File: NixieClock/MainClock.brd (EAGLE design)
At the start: 160 x 50 mm, 87 parts, among them IC1 MEGA8-P, IC2 74141N, IC3 NE555, Q1 MPSA 42, Q10 IRF740, Q11 BC547, Q12 MPSA 92, Q13 MPSA 42, Q14 MPSA 42, Q15 MPSA55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

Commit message: Placed all Parts
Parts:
- moved R15 191.4 mm to (86.0, 26.0)
- moved R37 172.6 mm to (70.0, 26.0), turned to 270 degrees
- moved NEON 167.2 mm to (76.0, 30.0), turned to 270 degrees
- moved C1 166.6 mm to (68.2, 13.9)
- moved R19 163.8 mm to (84.0, 46.0), turned to 90 degrees
- moved R36 158.5 mm to (72.0, 36.0), turned to 180 degrees
- moved D1 147.7 mm to (86.0, 34.0)
- moved R29 146.7 mm to (36.0, 14.0), turned to 180 degrees
- moved R30 145.7 mm to (14.0, 4.00), turned to 180 degrees
- moved Q15 139.0 mm to (100.0, 4.00), turned to 180 degrees
- moved Q11 136.0 mm to (91.9, 45.1), turned to 90 degrees
- moved R23 134.2 mm to (14.0, 16.0)
- moved R18 132.4 mm to (78.0, 43.5), turned to 90 degrees
- moved R17 129.5 mm to (86.0, 40.0), turned to 180 degrees
- moved R13 124.5 mm to (36.0, 22.0), turned to 180 degrees
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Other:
- board size 160 x 50 mm -> 172 x 52 mm

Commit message: Began Routing
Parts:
- moved +180V(TEST) 12.0 mm to (4.00, 4.00)
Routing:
- net N$34: track 0.00 -> 155.7 mm
- net N$16: track 0.00 -> 17.7 mm
- net N$11: track 0.00 -> 13.7 mm
- net N$15: track 0.00 -> 13.3 mm
- net N$55: track 0.00 -> 12.7 mm
- net N$33: track 0.00 -> 12.7 mm
- net N$32: track 0.00 -> 12.7 mm
- net N$31: track 0.00 -> 12.7 mm
- net N$30: track 0.00 -> 12.7 mm
- net N$29: track 0.00 -> 12.7 mm
- net N$12: track 0.00 -> 9.29 mm
- net N$14: track 0.00 -> 7.01 mm
- net N$40: track 0.00 -> 6.41 mm
- net N$39: track 0.00 -> 6.41 mm
- net N$38: track 0.00 -> 6.41 mm
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- added copper zone on layer 16, net VCC

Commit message: Routed the rest w the help of autorouter
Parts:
- moved R15 3.61 mm to (88.0, 29.0)
- moved D2 2.83 mm to (100.0, 8.00)
- moved CATHODE 1.50 mm to (76.0, 15.5)
- moved IC2 1.50 mm to (86.0, 13.5)
- moved NEON 1.00 mm to (76.0, 31.0)
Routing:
- net 9V: track 0.00 -> 185.0 mm
- net DIGITAL_PIN_13: track 0.00 -> 92.0 mm, vias 0 -> 2
- net DIGITAL_PIN_8: track 0.00 -> 91.6 mm, vias 0 -> 1
- net ANALOG_0: track 0.00 -> 89.7 mm
- net DIGITAL_PIN_10: track 0.00 -> 87.1 mm, vias 0 -> 2
- net DIGITAL_PIN_12: track 0.00 -> 85.8 mm, vias 0 -> 3
- net N$34: track 155.7 -> 237.0 mm
- net DIGITAL_PIN_11: track 0.00 -> 80.3 mm, vias 0 -> 1
- net DIGITAL_PIN_9: track 0.00 -> 76.8 mm, vias 0 -> 1
- net DIGITAL_PIN_5: track 0.00 -> 67.2 mm, vias 0 -> 3
- net N$7: track 0.00 -> 66.1 mm
- net DIGITAL_PIN_4: track 0.00 -> 62.2 mm, vias 0 -> 2
- net ANALOG_1: track 0.00 -> 56.4 mm, vias 0 -> 1
- net N$62: track 0.00 -> 55.9 mm
- net DIGITAL_PIN_2: track 0.00 -> 50.2 mm
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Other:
- board size 172 x 52 mm -> 172 x 54 mm

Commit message: Added Holes
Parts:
- moved GND 48.4 mm to (56.0, 50.0)
- moved +180V(TEST) 8.25 mm to (6.00, 12.0)
- moved 9V/12-35V-DC-IN 2.83 mm to (155.7, 8.31)
- moved 12-35V/9V 2.83 mm to (168.0, 30.0)
- moved ANODE 2.83 mm to (6.00, 28.0)
- moved BUZZER 2.83 mm to (158.0, 44.0)
- moved C1 2.83 mm to (70.2, 15.9)
- moved C10 2.83 mm to (148.0, 22.0)
- moved C2 2.83 mm to (114.0, 32.0)
- moved C3 2.83 mm to (106.0, 44.0)
- moved C4 2.83 mm to (82.0, 32.0)
- moved C5 2.83 mm to (136.0, 28.0)
- moved C6 2.83 mm to (142.0, 28.0)
- moved C7 2.83 mm to (148.0, 30.0)
- moved C8 2.83 mm to (138.0, 20.0)
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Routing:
- net N$49: track 36.7 -> 39.9 mm
- net DIGITAL_PIN_12: track 85.8 -> 87.5 mm
- net N$34: track 237.0 -> 237.9 mm
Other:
- board size 172 x 54 mm -> 174 x 56 mm

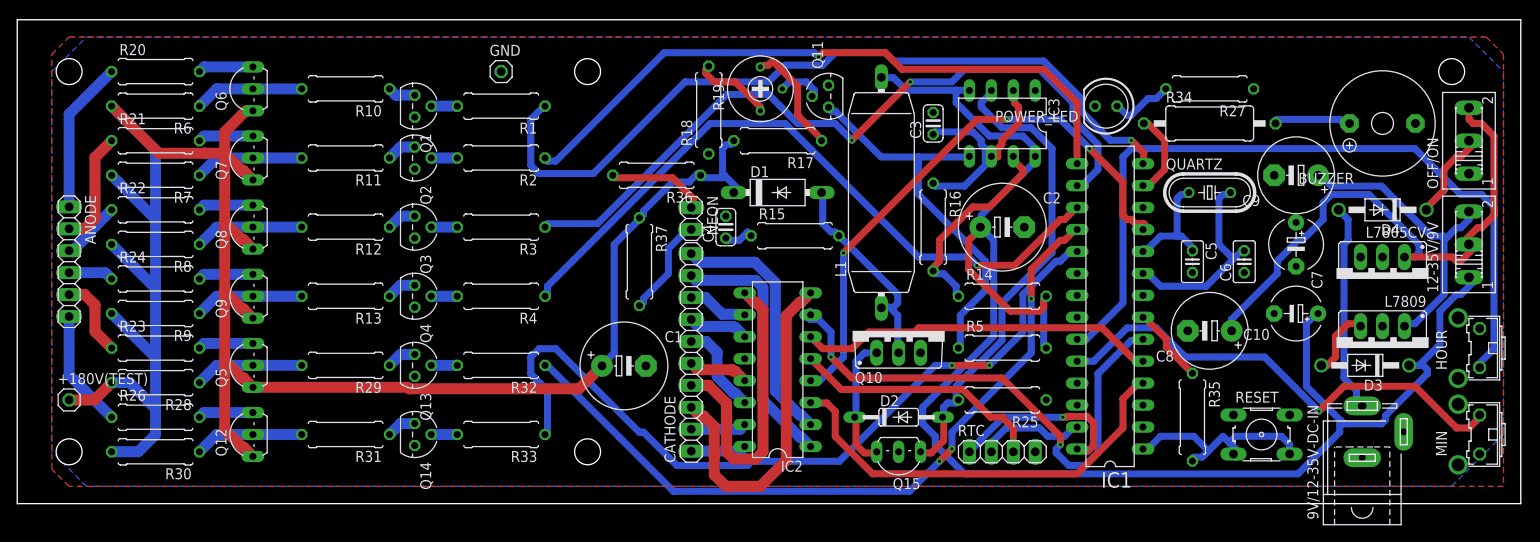
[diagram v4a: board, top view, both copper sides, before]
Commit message: Moved Names and Values so that they are easily readable
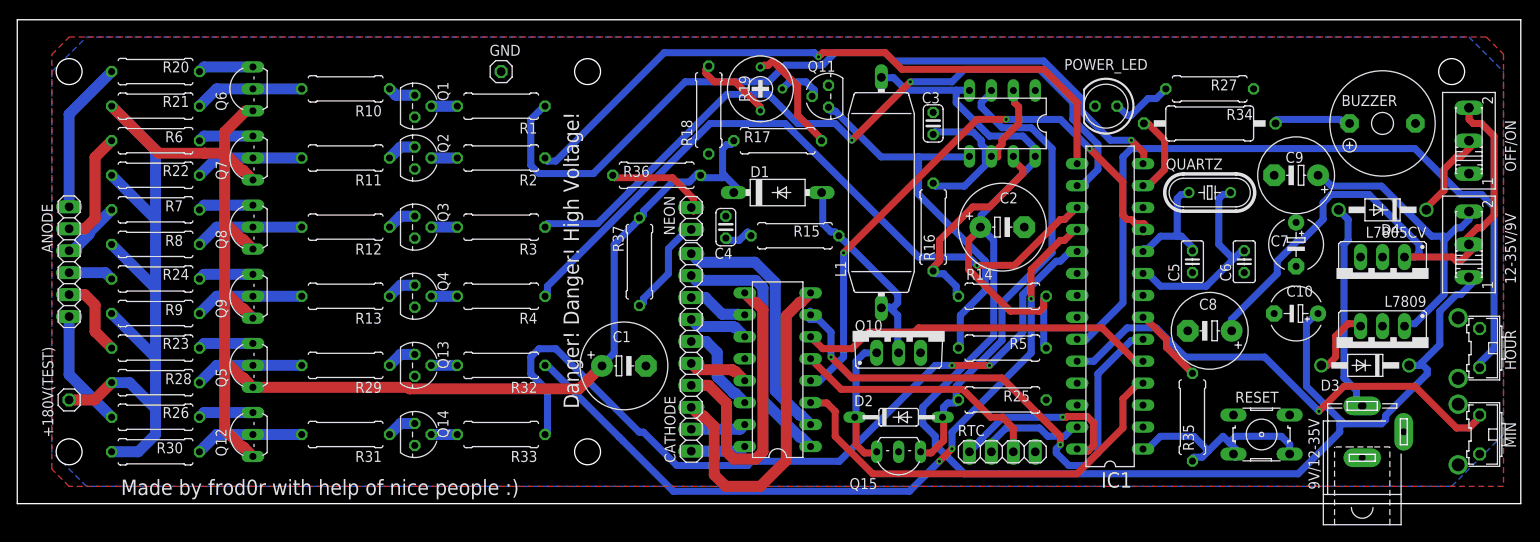
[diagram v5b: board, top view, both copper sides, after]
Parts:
- renumbered 9V/12-35V-DC-IN to 9V/12-35V
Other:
- board text added: "Danger! Danger! High Voltage!"
- board text added: "Made by frod0r with help of nice people :)"

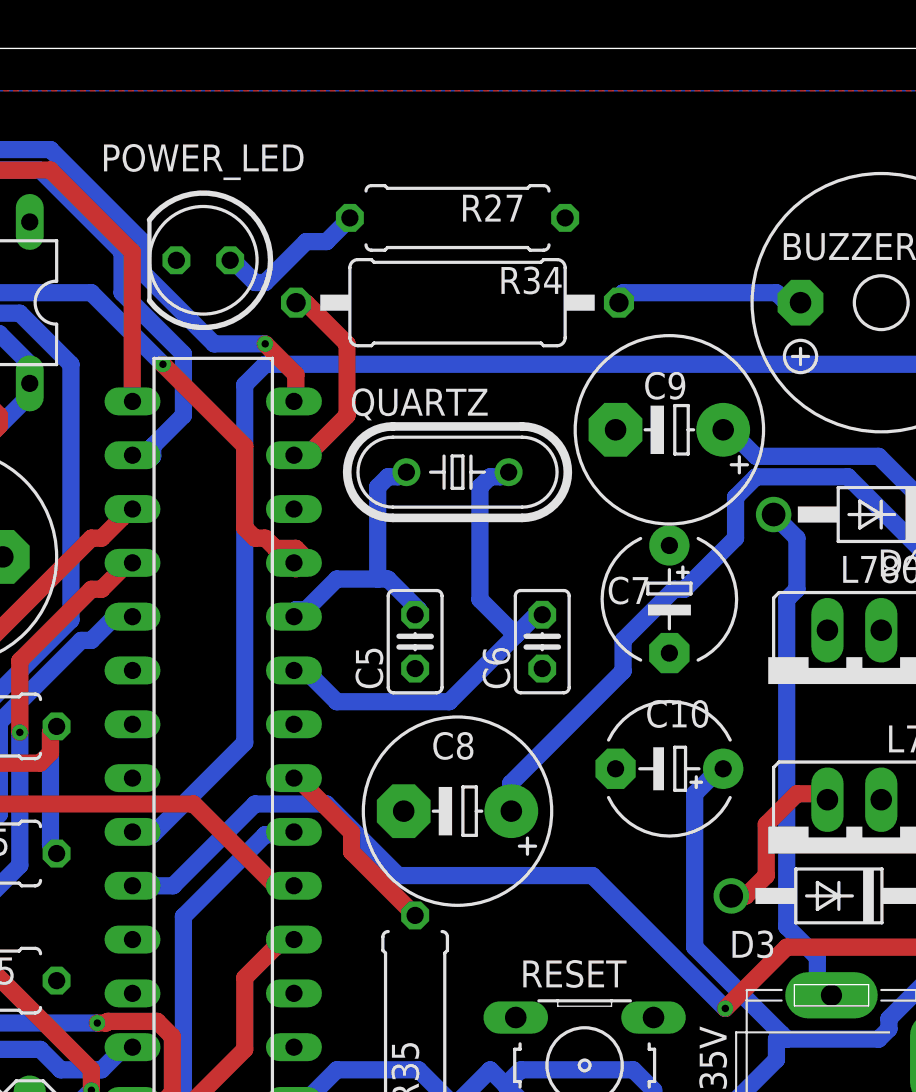
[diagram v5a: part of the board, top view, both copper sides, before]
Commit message: Added a button to the board and added the shield
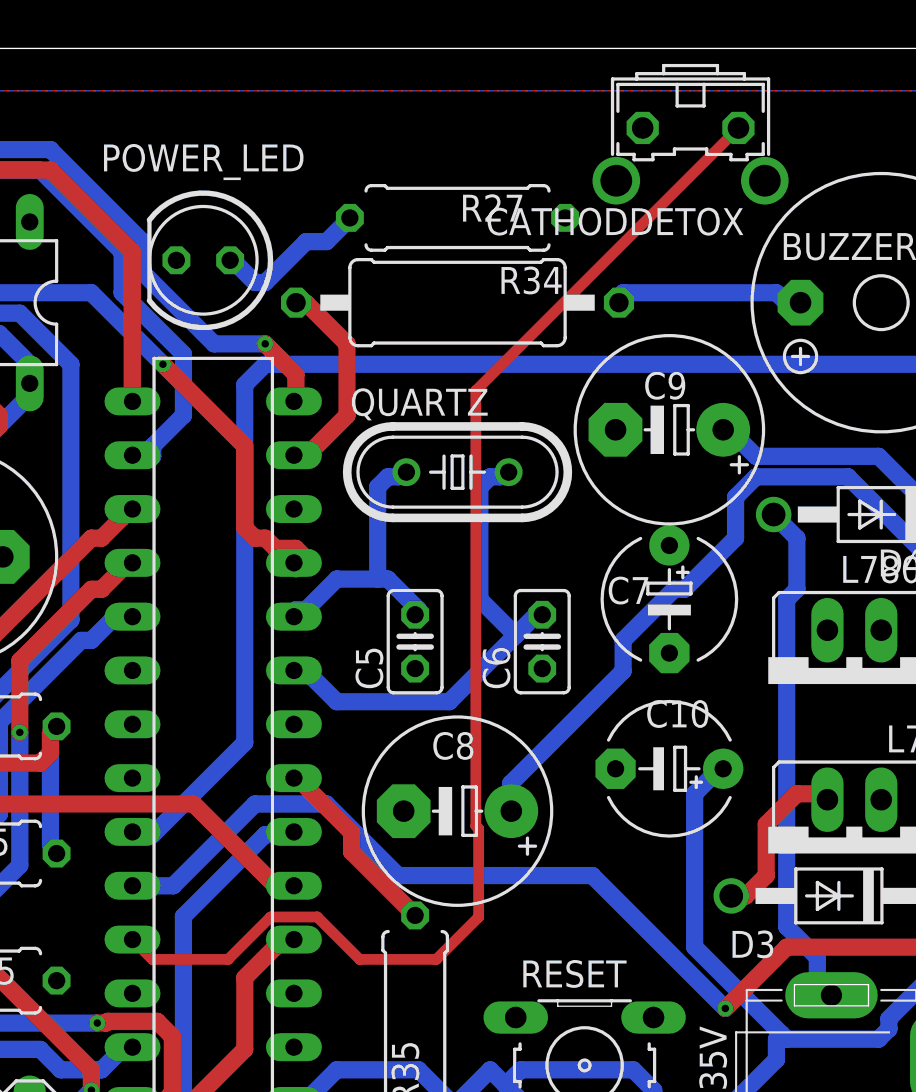
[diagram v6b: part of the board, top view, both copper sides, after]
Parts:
- added CATHODDETOX: (no value), switch-omron:B3F-31XX
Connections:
- new net ANALOG_2: CATHODDETOX.1, IC1.25
- net GND: now also CATHODDETOX.2
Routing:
- net ANALOG_2: track 0.00 -> 61.7 mm
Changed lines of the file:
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@@
 <element name="L7809" library="v-reg" library_urn="urn:adsk.eagle:library:409" package="78XXS" package3d_urn="urn:adsk.eagle:package:30342/1" value="" x="158" y="18" rot="R180"/>
 <element name="L7805CV" library="v-reg" library_urn="urn:adsk.eagle:library:409" package="78XXS" package3d_urn="urn:adsk.eagle:package:30342/1" value="" x="158" y="26" rot="R180"/>
+<element name="CATHODDETOX" library="switch-omron" library_urn="urn:adsk.eagle:library:377" package="B3F-31XX" package3d_urn="urn:adsk.eagle:package:27487/1" value="" x="149" y="51" rot="R180">
+<attribute name="MF" value="" x="149" y="51" size="1.778" layer="27" rot="R180" display="off"/>
+<attribute name="MPN" value="B3F-3100" x="149" y="51" size="1.778" layer="27" rot="R180" display="off"/>
+<attribute name="OC_FARNELL" value="959704" x="149" y="51" size="1.778" layer="27" rot="R180" display="off"/>
+<attribute name="OC_NEWARK" value="36M3582" x="149" y="51" size="1.778" layer="27" rot="R180" display="off"/>
+</element>
 </elements>
 <signals>
@@
 <contactref element="L7809" pad="GND"/>
 <contactref element="L7805CV" pad="GND"/>
+<contactref element="CATHODDETOX" pad="2"/>
 </signal>
 <signal name="VCC">
@@
 <wire x1="151.1234" y1="15.9954" x2="150.92" y2="16" width="0.8128" layer="1"/>
 </signal>
+<signal name="ANALOG_2">
+<contactref element="IC1" pad="25"/>
+<contactref element="CATHODDETOX" pad="1"/>
+<wire x1="138.8636" y1="19.30560625" x2="139" y2="19.16920625" width="0.508" layer="1"/>
+<wire x1="139" y1="19.16920625" x2="139" y2="15" width="0.508" layer="1"/>
+<wire x1="151.2606" y1="52.2446" x2="138.8636" y2="39.8476" width="0.508" layer="1"/>
+<wire x1="138.8636" y1="39.8476" x2="138.8636" y2="19.30560625" width="0.508" layer="1"/>
+<wire x1="139" y1="15" x2="137" y2="13" width="0.508" layer="1"/>
+<wire x1="123.6" y1="13" x2="122.66" y2="13.94" width="0.508" layer="1"/>
+<wire x1="131.3822875" y1="15.0068" x2="129.1777125" y2="15.0068" width="0.508" layer="1"/>
+<wire x1="133.3890875" y1="13" x2="131.3822875" y2="15.0068" width="0.508" layer="1"/>
+<wire x1="127.1709125" y1="13" x2="123.6" y2="13" width="0.508" layer="1"/>
+<wire x1="129.1777125" y1="15.0068" x2="127.1709125" y2="13" width="0.508" layer="1"/>
+<wire x1="137" y1="13" x2="133.3890875" y2="13" width="0.508" layer="1"/>
+</signal>
 </signals>

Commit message: applied rules to main
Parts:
- moved C3 3.50 mm to (106.0, 40.5)
- moved POWER_LED 2.06 mm to (125.5, 48.0), turned to 270 degrees
- moved GND 0.50 mm to (56.0, 50.5)
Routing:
- net GND: track 0.00 -> 24.4 mm, vias 0 -> 3
- net DIGITAL_PIN_5: track 67.2 -> 80.9 mm
- net VCC: track 38.5 -> 51.8 mm
- net N$59: track 45.3 -> 55.5 mm, vias 0 -> 1
- net N$54: track 27.5 -> 19.3 mm
- net N$49: track 39.9 -> 47.6 mm
- net ANALOG_1: track 56.4 -> 62.9 mm
- net DIGITAL_PIN_2: track 50.2 -> 56.7 mm
- net DIGITAL_PIN_8: track 91.6 -> 85.5 mm, vias 1 -> 0
- net SCL: track 21.3 -> 15.3 mm, vias 1 -> 0
- net N$34: track 237.9 -> 233.2 mm
- net 9V: track 185.0 -> 189.1 mm
- net N$48: track 34.8 -> 38.1 mm
- net DIGITAL_PIN_10: track 87.1 -> 90.1 mm, vias 2 -> 0
- net N$51: track 29.3 -> 31.8 mm
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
